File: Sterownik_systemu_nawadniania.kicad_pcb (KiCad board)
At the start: 2 copper layers, 0 parts

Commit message: footprints
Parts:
- added C1: 100nF, Capacitor_SMD:C_0603_1608Metric, F.Cu at (110.5, 68.3)
- added C10: 100nF, Capacitor_SMD:C_0603_1608Metric, F.Cu at (143.9, 44.7)
- added C11: 100nF, Capacitor_SMD:C_0603_1608Metric, F.Cu at (159.8, 21.7)
- added C12: 100nF, Capacitor_SMD:C_0603_1608Metric, F.Cu at (121.5, 58.9)
- added C13: 100nF, Capacitor_SMD:C_0603_1608Metric, F.Cu at (121.5, 61.4)
- added C14: 4.7uF, Capacitor_SMD:C_0603_1608Metric, F.Cu at (163.8, 21.7)
- added C15: 100nF, Capacitor_SMD:C_0603_1608Metric, F.Cu at (132.6, 56.0)
- added C16: 1uF, Capacitor_SMD:C_0603_1608Metric, F.Cu at (157.0, 33.5)
- added C17: 1uF, Capacitor_SMD:C_0603_1608Metric, F.Cu at (129.5, 61.0)
- added C18: 100nF, Capacitor_SMD:C_0603_1608Metric, F.Cu at (117.5, 62.3)
- added C19: 100nF, Capacitor_SMD:C_0603_1608Metric, F.Cu at (121.5, 66.4)
- added C2: 1uF, Capacitor_SMD:C_0603_1608Metric, F.Cu at (153.0, 36.0)
- added C20: 22uF, Capacitor_SMD:C_2220_5650Metric, F.Cu at (146.8, 34.9)
- added C21: 22uF, Capacitor_SMD:C_2220_5650Metric, F.Cu at (122.3, 54.2)
- added C22: 100nF, Capacitor_SMD:C_0603_1608Metric, F.Cu at (193.4, 40.7)
- added C3: 4.7uF, Capacitor_SMD:C_0603_1608Metric, F.Cu at (106.5, 68.3)
- added C4: 100nF, Capacitor_SMD:C_0603_1608Metric, F.Cu at (157.0, 31.0)
- added C5: 100nF, Capacitor_SMD:C_0603_1608Metric, F.Cu at (159.8, 26.7)
- added C6: 14pF, Capacitor_SMD:C_0402_1005Metric, F.Cu at (75.4, 69.8)
- added C7: 14pF, Capacitor_SMD:C_0402_1005Metric, F.Cu at (113.9, 68.1)
- added C8: 10nF, Capacitor_SMD:C_0603_1608Metric, F.Cu at (143.9, 42.2)
- added C9: 1uF, Capacitor_SMD:C_0603_1608Metric, F.Cu at (121.5, 63.9)
- added D1: 1N4007G, 1N4007G:DIOAD1036W78L470D235, F.Cu at (303.5, 9.14)
- added D2: 1N4007G, 1N4007G:DIOAD1036W78L470D235, F.Cu at (264.9, 8.38)
- added D3: 1N4007G, 1N4007G:DIOAD1036W78L470D235, F.Cu at (215.6, 14.5)
- added D4: 1N4007G, 1N4007G:DIOAD1036W78L470D235, F.Cu at (172.7, 8.89)
- added IC1: STM32F030C6T6, STM32F030:QFP50P900X900X160-48N, F.Cu at (135.9, 25.4)
- added J1: CON-SOCJ-2155, CON-SOCJ-2155:GRAVITECH_CON-SOCJ-2155, F.Cu at (170.3, 102.1)
- added J2: Conn_01x05_Male, Connector_PinHeader_2.54mm:PinHeader_1x05_P2.54mm_Vertical, F.Cu at (118.4, 21.1)
- added J3: Conn_01x16_Female, Connector_PinSocket_2.54mm:PinSocket_1x16_P2.54mm_Vertical, F.Cu at (57.1, 27.2)
- added J4: Screw_Terminal_01x02, TerminalBlock:TerminalBlock_bornier-2_P5.08mm, F.Cu at (311.4, 24.6)
- added J5: Screw_Terminal_01x02, TerminalBlock:TerminalBlock_bornier-2_P5.08mm, F.Cu at (303.0, -21.1)
- added J6: Screw_Terminal_01x02, TerminalBlock:TerminalBlock_bornier-2_P5.08mm, F.Cu at (260.9, -21.8)
- added J7: Screw_Terminal_01x02, TerminalBlock:TerminalBlock_bornier-2_P5.08mm, F.Cu at (214.4, -24.6)
- added J8: Screw_Terminal_01x02, TerminalBlock:TerminalBlock_bornier-2_P5.08mm, F.Cu at (169.7, -23.1)
- added K1: 1461103-1, Project_lic_footprints_AM:OJ_OJE, F.Cu at (295.0, -4.16)
- added K2: 1461103-1, Project_lic_footprints_AM:OJ_OJE, F.Cu at (256.9, -4.41)
- added K3: 1461103-1, Project_lic_footprints_AM:OJ_OJE, F.Cu at (206.9, -5.68)
- added K4: 1461103-1, Project_lic_footprints_AM:OJ_OJE, F.Cu at (181.8, -14.4)
- added L1: 12uH, ul_RLB0712-120KL:RLB0712-120KL, F.Cu at (110.6, 52.7)
- added Q1: ZTX450, eec:TO92250P510H770-3, F.Cu at (304.5, 1.02)
- added Q2: ZTX450, eec:TO92250P510H770-3, F.Cu at (265.4, 0.00)
- added Q3: ZTX450, eec:TO92250P510H770-3, F.Cu at (215.9, -0.25)
- added Q4: ZTX450, eec:TO92250P510H770-3, F.Cu at (171.9, 0.00)
- added R1: 10k, Resistor_SMD:R_0603_1608Metric, F.Cu at (128.6, 53.5)
- added R10: 1k, Resistor_SMD:R_0603_1608Metric, F.Cu at (167.9, 21.7)
- added R11: 10k, Resistor_SMD:R_0603_1608Metric, F.Cu at (125.5, 61.4)
- added R12: 10k, Resistor_SMD:R_0603_1608Metric, F.Cu at (163.8, 24.2)
- added R13: 1k, Resistor_SMD:R_0603_1608Metric, F.Cu at (125.5, 58.9)
- added R14: 1k, Resistor_SMD:R_0603_1608Metric, F.Cu at (144.5, 39.7)
- added R15: 10k, Resistor_SMD:R_0603_1608Metric, F.Cu at (128.6, 56.0)
- added R16: 10k, Resistor_SMD:R_0603_1608Metric, F.Cu at (117.5, 64.8)
- added R17: 10k, Resistor_SMD:R_0603_1608Metric, F.Cu at (132.6, 53.5)
- added R18: 10k, Resistor_SMD:R_0603_1608Metric, F.Cu at (147.9, 42.2)
- added R19: 10k, Resistor_SMD:R_0603_1608Metric, F.Cu at (148.6, 39.7)
- added R2: 10k, Resistor_SMD:R_0603_1608Metric, F.Cu at (117.5, 67.3)
- added R20: 51k, Resistor_SMD:R_0603_1608Metric, F.Cu at (159.8, 24.2)
- added R21: 22.1k, Resistor_SMD:R_0603_1608Metric, F.Cu at (153.0, 31.0)
- added R22: 100, Resistor_SMD:R_0603_1608Metric, F.Cu at (153.0, 33.5)
- added R23: 220, Resistor_SMD:R_0603_1608Metric, F.Cu at (303.5, 6.10)
- added R24: 220, Resistor_SMD:R_0603_1608Metric, F.Cu at (265.9, 5.33)
- added R25: 10k, Resistor_SMD:R_0603_1608Metric, F.Cu at (200.4, 24.6)
- added R26: 1k, Resistor_SMD:R_0603_1608Metric, F.Cu at (239.5, 53.1)
- added R27: 220, Resistor_SMD:R_0603_1608Metric, F.Cu at (215.9, 6.35)
- added R28: 220, Resistor_SMD:R_0603_1608Metric, F.Cu at (172.0, 5.59)
- added R29: 220, Resistor_SMD:R_0603_1608Metric, F.Cu at (195.3, 30.7)
- added R3: 1k, Resistor_SMD:R_0603_1608Metric, F.Cu at (121.5, 69.0)
- added R30: 220, Resistor_SMD:R_0603_1608Metric, F.Cu at (189.4, 38.2)
- added R31: 220, Resistor_SMD:R_0603_1608Metric, F.Cu at (189.4, 35.7)
- added R4: 1k, Resistor_SMD:R_0603_1608Metric, F.Cu at (129.5, 58.5)
- added R5: 220, Resistor_SMD:R_0603_1608Metric, F.Cu at (188.9, 25.7)
- added R6: 1.5k, Resistor_SMD:R_0603_1608Metric, F.Cu at (117.5, 59.8)
- added R7: 10k, Resistor_SMD:R_0603_1608Metric, F.Cu at (125.5, 63.9)
- added R8: 10k, Resistor_SMD:R_0603_1608Metric, F.Cu at (163.8, 26.7)
- added R9: 1k, Resistor_SMD:R_0603_1608Metric, F.Cu at (136.6, 53.5)
- added RV1: 10k, 3362P-1-103LF:TRIM_3362P-1-103LF, F.Cu at (42.4, 30.5)
- added SW1: SW_SPST, Project_lic_footprints_AM:430156043736_AM, F.Cu at (92.8, 92.5)
- added SW2: SW_SPST, Project_lic_footprints_AM:430156043736_AM, F.Cu at (77.1, 92.7)
- added SW3: SW_SPST, Project_lic_footprints_AM:430156043736_AM, F.Cu at (60.8, 108.7)
- added SW4: SW_SPST, Project_lic_footprints_AM:430156043736_AM, F.Cu at (77.1, 106.5)
- added SW5: SW_SPST, Project_lic_footprints_AM:430156043736_AM, F.Cu at (60.3, 93.0)
- added SW6: SW_SPST, Project_lic_footprints_AM:430156043736_AM, F.Cu at (92.3, 105.7)
- added SW7: 25336NA, eec3:Apem_Inc.-25336NA-MFG, F.Cu at (189.7, 102.6)
- added U1: ESP-12E, RF_Module:ESP-12E, F.Cu at (83.3, 22.9)
- added U2: LMR50410XDBVR, eec2:Texas_Instruments-DBV0006A-0-0-MFG, F.Cu at (216.7, 104.6)
- added U3: LTV-844, Package_DIP:DIP-16_W7.62mm, F.Cu at (238.0, 16.8)
- added Y1: Crystal, ECS-80-12-30Q-DS-TR:XTAL_ECS-80-18-30-JGN-TR, F.Cu at (91.4, 79.2)

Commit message: adj
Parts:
- moved J5 348.0 mm to (21.6, 183.6), turned to 90 degrees
- moved Q1 308.3 mm to (56.9, 184.7), turned to -90 degrees
- moved K1 307.1 mm to (46.4, 176.1), turned to 180 degrees
- moved D1 305.7 mm to (51.3, 181.9), turned to 90 degrees
- moved J6 305.3 mm to (21.8, 168.1), turned to 90 degrees
- moved R23 301.6 mm to (55.9, 178.3), turned to -90 degrees
- moved Q2 268.0 mm to (55.9, 167.1), turned to -90 degrees
- moved K2 266.6 mm to (47.1, 160.1), turned to 180 degrees
- moved D2 265.0 mm to (50.8, 164.6), turned to 90 degrees
- moved R24 261.4 mm to (55.6, 160.6), turned to -90 degrees
- moved J7 260.5 mm to (22.1, 151.1), turned to 90 degrees
- moved Q3 220.0 mm to (56.6, 151.6), turned to -90 degrees
- moved K3 218.3 mm to (47.4, 143.4), turned to 180 degrees
- moved J8 214.7 mm to (22.4, 133.1), turned to 90 degrees
- moved U3 212.5 mm to (75.9, 154.2), turned to 180 degrees
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
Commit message: group
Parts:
- moved C18 180.4 mm to (272.4, 154.7), turned to 180 degrees
- moved R21 172.6 mm to (267.3, 160.3), turned to 90 degrees
- moved C19 170.7 mm to (267.1, 155.6), turned to 90 degrees
- moved R20 170.5 mm to (262.4, 160.4), turned to -90 degrees
- moved C17 168.3 mm to (272.4, 150.0), turned to 180 degrees
- moved J3 89.3 mm to (146.4, 30.3), turned to -90 degrees
- moved R17 83.8 mm to (213.9, 33.0)
- moved R22 77.9 mm to (111.9, 38.6), turned to 90 degrees
- moved R16 76.1 mm to (186.7, 33.3)
- moved C8 68.1 mm to (79.5, 64.3)
- moved R18 65.9 mm to (213.9, 42.2), turned to -90 degrees
- moved R19 65.4 mm to (213.9, 36.8)
- moved R15 64.1 mm to (186.7, 29.0)
- moved C20 62.4 mm to (249.3, 158.8), turned to 180 degrees
- moved C15 53.0 mm to (185.2, 49.5)
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
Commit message: update
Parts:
- moved C7 73.2 mm to (65.8, 120.7)
- moved IC1 73.2 mm to (92.3, 119.1)
- moved Y1 73.2 mm to (73.7, 117.6)
- moved C2 73.2 mm to (83.1, 122.4)
- moved R6 73.2 mm to (83.2, 117.3)
- moved C6 73.2 mm to (65.6, 115.6)
- moved J4 70.5 mm to (207.9, 101.3)
- moved C22 68.5 mm to (201.4, 99.3)
- moved R26 68.3 mm to (201.4, 103.9)
- moved R25 68.2 mm to (201.4, 108.5)
- moved C8 63.2 mm to (63.2, 125.3), turned to 180 degrees
- moved C9 59.1 mm to (56.4, 125.3)
- moved R17 55.4 mm to (195.1, 85.1), turned to -90 degrees
- moved R19 52.5 mm to (193.2, 85.1), turned to -90 degrees
- moved R18 49.1 mm to (190.1, 85.1), turned to 180 degrees
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
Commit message: lab 14.11
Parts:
- moved RV1 129.2 mm to (179.7, 63.8)
- moved J1 92.1 mm to (166.1, 110.2)
- moved C17 89.7 mm to (163.7, 118.2)
- moved C18 89.7 mm to (163.7, 122.7)
- moved C19 89.7 mm to (157.6, 122.4)
- moved R20 89.7 mm to (152.9, 127.2)
- moved R21 89.7 mm to (157.9, 127.1)
- moved SW7 89.7 mm to (171.2, 122.8)
- moved U2 89.7 mm to (163.7, 128.0)
- moved L1 88.8 mm to (156.6, 99.2)
- moved C21 88.6 mm to (148.1, 97.5), turned to -90 degrees
- moved C20 87.1 mm to (149.5, 106.2), turned to -90 degrees
- moved D1 85.9 mm to (122.7, 117.7)
- moved D4 85.9 mm to (122.6, 74.3)
- moved J5 85.9 mm to (97.8, 120.4)
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
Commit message: stable1
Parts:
- moved R12 108.4 mm to (141.1, 83.1)
- moved R11 107.7 mm to (130.1, 83.1)
- moved R8 107.6 mm to (119.2, 83.1)
- moved R10 103.6 mm to (123.0, 83.1), turned to 180 degrees
- moved R14 103.2 mm to (144.9, 83.1), turned to 180 degrees
- moved R13 103.2 mm to (133.9, 83.1), turned to 180 degrees
- moved R7 101.9 mm to (141.0, 71.5)
- moved C1 101.6 mm to (134.2, 111.0), turned to 90 degrees
- moved R4 101.3 mm to (133.9, 71.5), turned to 180 degrees
- moved C11 100.2 mm to (126.8, 83.1)
- moved SW4 98.7 mm to (126.0, 90.4)
- moved C12 98.6 mm to (137.8, 83.1)
- moved C13 98.2 mm to (148.7, 83.1)
- moved SW1 97.1 mm to (126.0, 78.8)
- moved R9 97.1 mm to (144.8, 71.5), turned to 180 degrees
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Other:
- board outline added: 77.7 x 134.2 mm
- board text added: "GND"
- board text added: "NRST"
- board text added: "SWCLK"
- board text added: "SWDIO"
- board text added: "VDD"

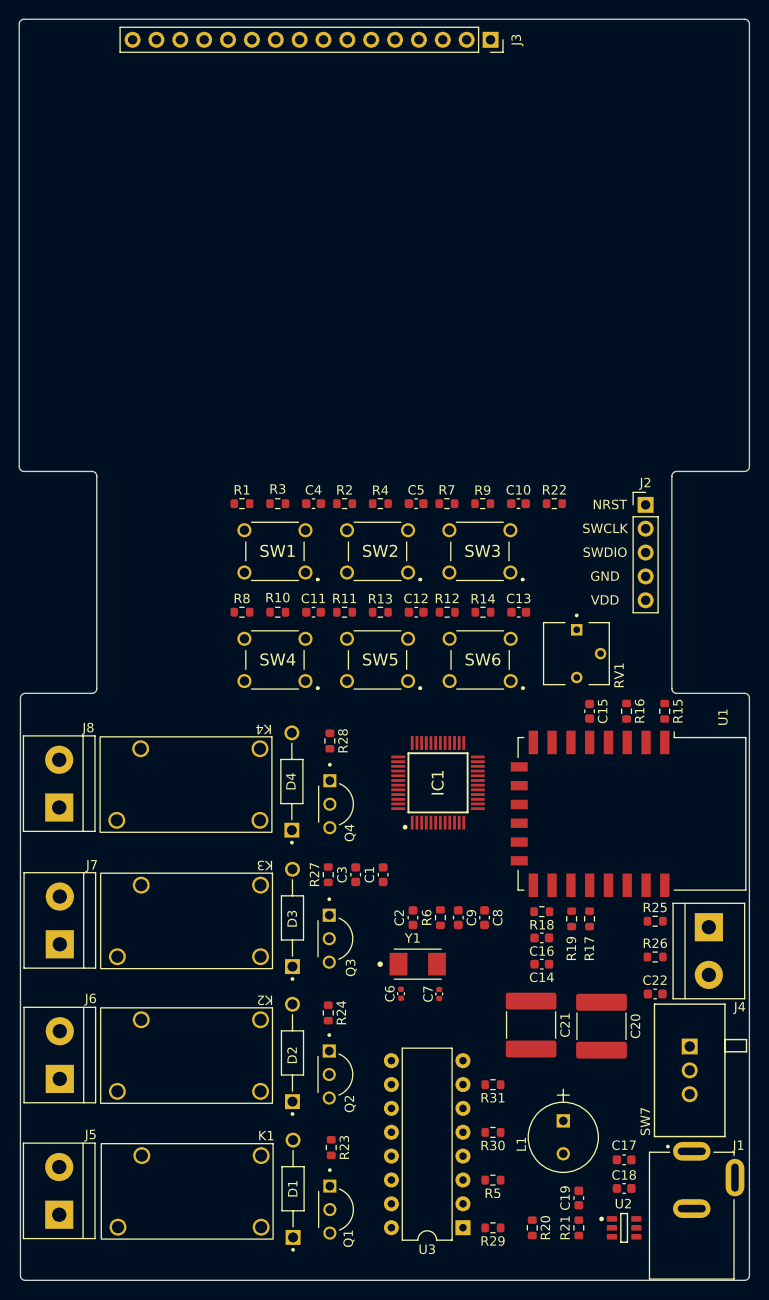
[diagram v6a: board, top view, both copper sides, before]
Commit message: Routing with ground field
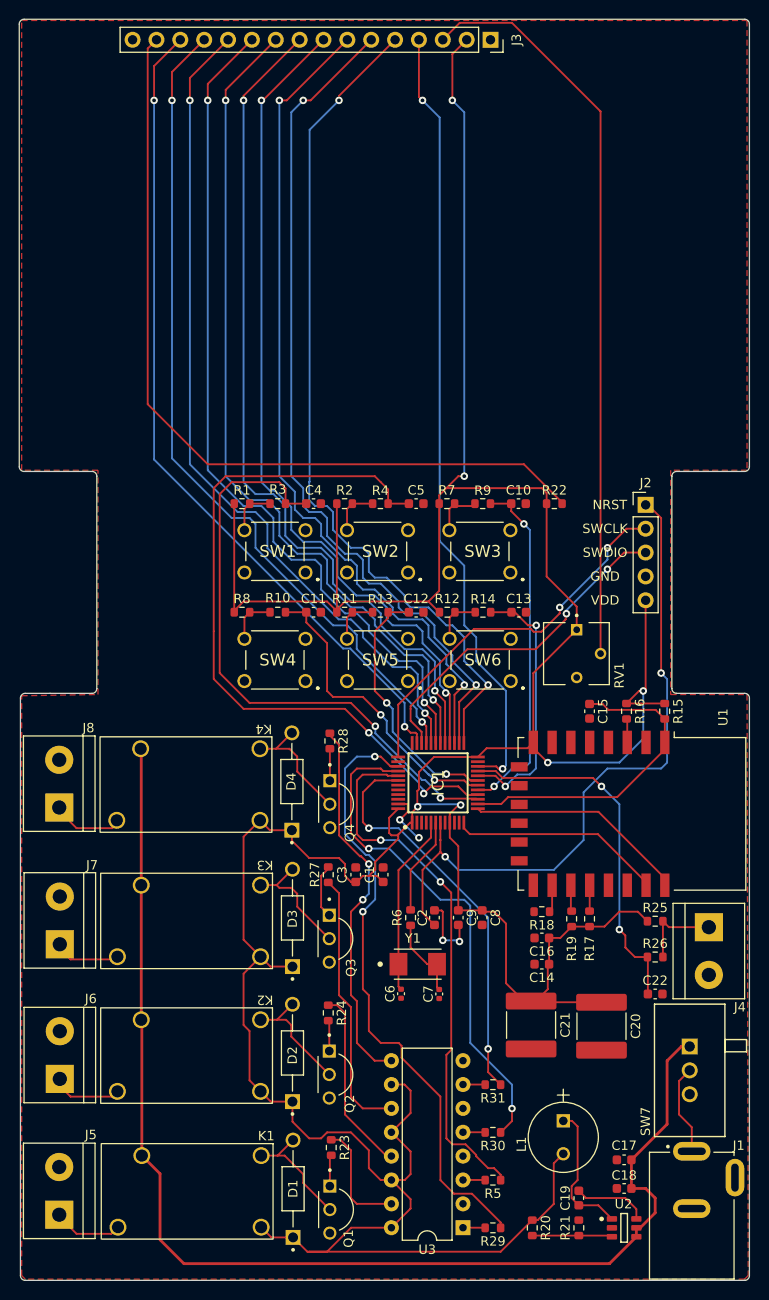
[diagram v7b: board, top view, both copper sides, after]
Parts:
- moved R6 3.18 mm to (137.2, 115.6)
- moved C2 2.29 mm to (139.7, 115.6)
- moved C8 0.25 mm to (144.8, 115.6)
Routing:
- net VDD: track 0.00 -> 422.8 mm, vias 0 -> 6
- net +24V: track 0.00 -> 132.4 mm
- net /DISP_RW: track 0.00 -> 91.3 mm, vias 0 -> 2
- net /DISP_DB4: track 0.00 -> 91.3 mm, vias 0 -> 2
- net /DISP_DB2: track 0.00 -> 91.1 mm, vias 0 -> 2
- net /DISP_E: track 0.00 -> 91.1 mm, vias 0 -> 2
- net /DISP_DB3: track 0.00 -> 91.0 mm, vias 0 -> 2
- net /DISP_DB1: track 0.00 -> 90.5 mm, vias 0 -> 2
- net /DISP_DB0: track 0.00 -> 90.3 mm, vias 0 -> 2
- net /DISP_DB5: track 0.00 -> 90.2 mm, vias 0 -> 2
- net /DISP_DB6: track 0.00 -> 89.5 mm, vias 0 -> 2
- net /DISP_DB7: track 0.00 -> 88.4 mm, vias 0 -> 2
- net Net-(J3-Pad15): track 0.00 -> 87.8 mm
- net /DISP_RS: track 0.00 -> 84.3 mm, vias 0 -> 2
- net /DISP_Contrast: track 0.00 -> 79.2 mm
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- added copper zone on F.Cu, net GND

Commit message: Lab 21.11
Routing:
- net /Valve_2: track 54.0 -> 52.6 mm
- net /Valve_1: track 65.9 -> 64.8 mm
- net Net-(J1-Pad1): track 9.65 -> 10.7 mm
- net /Valve_3: track 57.4 -> 56.5 mm
- net Net-(J5-Pad1): track 7.50 -> 6.86 mm
- net Net-(J6-Pad1): track 7.57 -> 8.16 mm
- net Net-(D2-PadA): track 12.8 -> 12.2 mm
- net Net-(J7-Pad1): track 7.19 -> 6.68 mm
- removed copper zone on F.Cu, net GND
